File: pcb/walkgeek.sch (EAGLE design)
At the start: 124 parts, among them M1 NOKIA1100_VIBRATOR, X1 NOKIA1100_EXT_CONN, X2 MICROSD_CONN

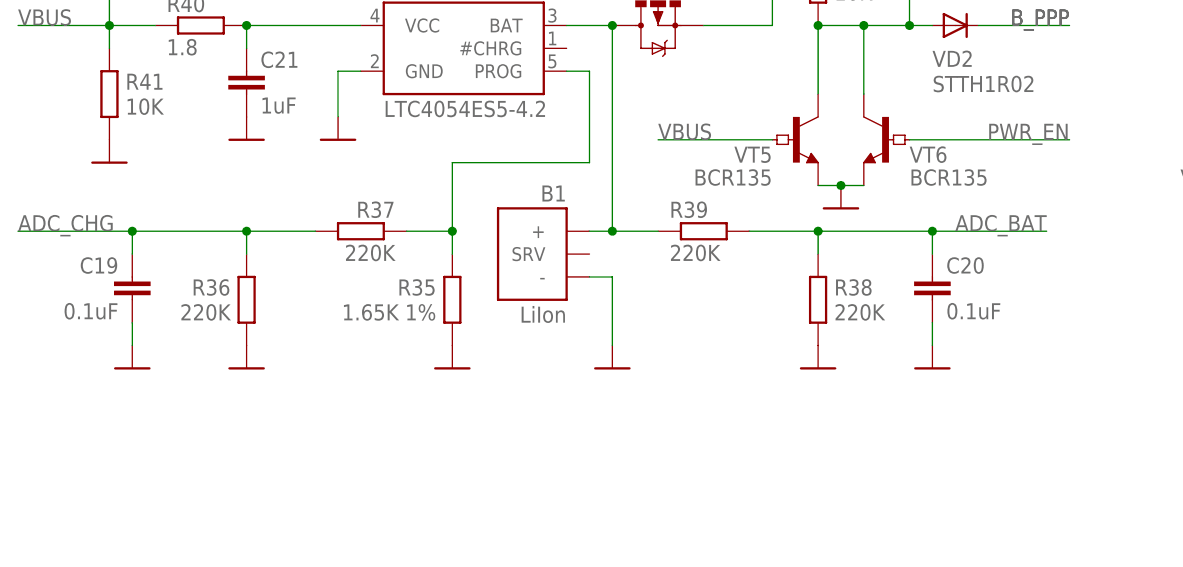
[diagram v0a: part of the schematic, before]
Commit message: Ported OPUS
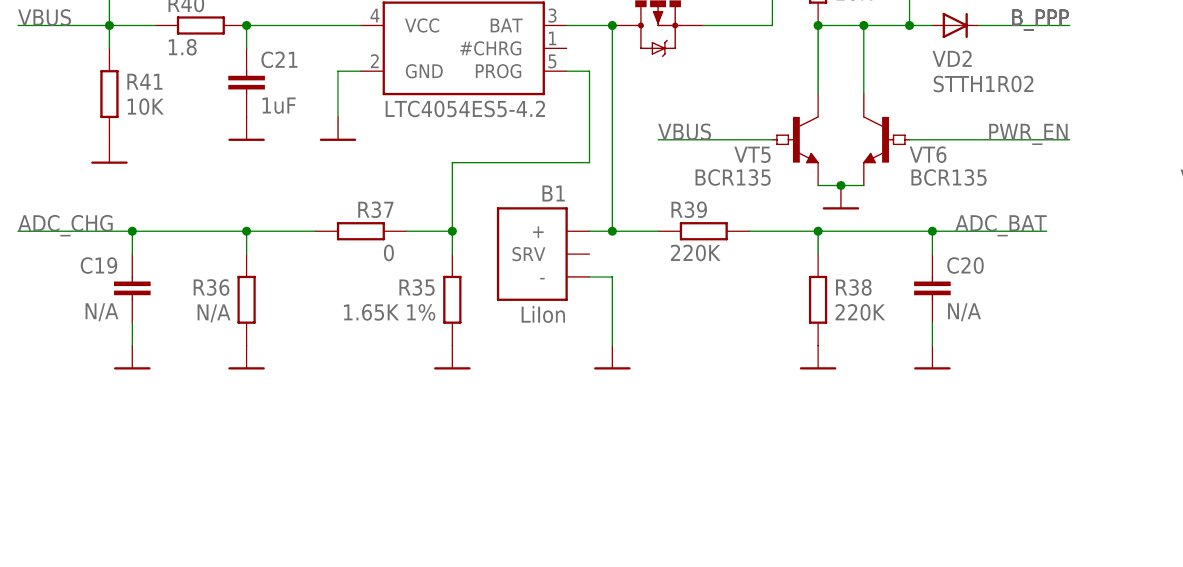
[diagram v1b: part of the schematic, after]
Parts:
- C19, C20: value 0.1uF -> N/A
- R36: value 220K -> N/A
- R37: value 220K -> 0
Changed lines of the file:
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@@
 <setting verticaltext="up"/>
 </settings>
-<grid distance="0.05" unitdist="inch" unit="inch" style="lines" multiple="1" display="no" altdistance="0.01" altunitdist="inch" altunit="inch"/>
+<grid distance="0.1" unitdist="inch" unit="inch" style="lines" multiple="1" display="no" altdistance="0.01" altunitdist="inch" altunit="inch"/>
 <layers>
 <layer number="1" name="Top" color="4" fill="1" visible="no" active="no"/>
@@
 <part name="DD3" library="walkgeek-eagle" deviceset="LTC4054ES5-4.2" device=""/>
 <part name="R35" library="walkgeek-eagle" deviceset="R-EU_" device="R0805" value="1.65K 1%"/>
-<part name="R36" library="walkgeek-eagle" deviceset="R-EU_" device="R0805" value="220K"/>
-<part name="R37" library="walkgeek-eagle" deviceset="R-EU_" device="R0805" value="220K"/>
+<part name="R36" library="walkgeek-eagle" deviceset="R-EU_" device="R0805" value="N/A"/>
+<part name="R37" library="walkgeek-eagle" deviceset="R-EU_" device="R0805" value="0"/>
 <part name="GND17" library="supply1" deviceset="GND" device=""/>
 <part name="GND19" library="supply1" deviceset="GND" device=""/>
 <part name="GND20" library="supply1" deviceset="GND" device=""/>
-<part name="C19" library="walkgeek-eagle" deviceset="C-EU" device="C0805" value="0.1uF"/>
+<part name="C19" library="walkgeek-eagle" deviceset="C-EU" device="C0805" value="N/A"/>
 <part name="GND21" library="supply1" deviceset="GND" device=""/>
 <part name="GND22" library="supply1" deviceset="GND" device=""/>
@@
 <part name="R39" library="walkgeek-eagle" deviceset="R-EU_" device="R0805" value="220K"/>
 <part name="GND23" library="supply1" deviceset="GND" device=""/>
-<part name="C20" library="walkgeek-eagle" deviceset="C-EU" device="C0805" value="0.1uF"/>
+<part name="C20" library="walkgeek-eagle" deviceset="C-EU" device="C0805" value="N/A"/>
 <part name="GND24" library="supply1" deviceset="GND" device=""/>
 <part name="C21" library="walkgeek-eagle" deviceset="C-EU" device="C0805" value="1uF"/>

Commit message: PowerManager fixes
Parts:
- removed C19, C20: N/A, walkgeek-eagle:C-EUC0805
- removed R36: N/A, walkgeek-eagle:R-EU_R0805
- removed R37: 0, walkgeek-eagle:R-EU_R0805
- R35: value 1.65K 1% -> 2K 1%
- R38, R39: value 220K -> 10K 1%
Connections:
- removed net N$15: DD3.PROG, R35.2, R37.1
- net ADC_BAT: no longer C20.1
- net ADC_CHG: now also DD3.PROG, R35.2; no longer C19.1, R36.2, R37.2
- net GND: no longer C19.2, C20.2, R36.1
- net N$17: now also R39.1
- net VBAT0: no longer R39.1
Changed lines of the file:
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@@
 <part name="R34" library="walkgeek-eagle" deviceset="R-EU_" device="R0805" value="47K"/>
 <part name="DD3" library="walkgeek-eagle" deviceset="LTC4054ES5-4.2" device=""/>
-<part name="R35" library="walkgeek-eagle" deviceset="R-EU_" device="R0805" value="1.65K 1%"/>
-<part name="R36" library="walkgeek-eagle" deviceset="R-EU_" device="R0805" value="N/A"/>
-<part name="R37" library="walkgeek-eagle" deviceset="R-EU_" device="R0805" value="0"/>
+<part name="R35" library="walkgeek-eagle" deviceset="R-EU_" device="R0805" value="2K 1%"/>
 <part name="GND17" library="supply1" deviceset="GND" device=""/>
-<part name="GND19" library="supply1" deviceset="GND" device=""/>
 <part name="GND20" library="supply1" deviceset="GND" device=""/>
-<part name="C19" library="walkgeek-eagle" deviceset="C-EU" device="C0805" value="N/A"/>
-<part name="GND21" library="supply1" deviceset="GND" device=""/>
 <part name="GND22" library="supply1" deviceset="GND" device=""/>
-<part name="R38" library="walkgeek-eagle" deviceset="R-EU_" device="R0805" value="220K"/>
-<part name="R39" library="walkgeek-eagle" deviceset="R-EU_" device="R0805" value="220K"/>
+<part name="R38" library="walkgeek-eagle" deviceset="R-EU_" device="R0805" value="10K 1%"/>
+<part name="R39" library="walkgeek-eagle" deviceset="R-EU_" device="R0805" value="10K 1%"/>
 <part name="GND23" library="supply1" deviceset="GND" device=""/>
-<part name="C20" library="walkgeek-eagle" deviceset="C-EU" device="C0805" value="N/A"/>
-<part name="GND24" library="supply1" deviceset="GND" device=""/>
 <part name="C21" library="walkgeek-eagle" deviceset="C-EU" device="C0805" value="1uF"/>
 <part name="GND25" library="supply1" deviceset="GND" device=""/>
@@
 <attribute name="VALUE" x="488.442" y="207.772" size="1.778" layer="96" rot="R180"/>
 </instance>
-<instance part="R36" gate="G$1" x="467.36" y="208.28" smashed="yes" rot="MR90">
-<attribute name="NAME" x="465.582" y="208.7626" size="1.778" layer="95" rot="MR0"/>
-<attribute name="VALUE" x="465.582" y="207.772" size="1.778" layer="96" rot="R180"/>
-</instance>
-<instance part="R37" gate="G$1" x="480.06" y="215.9" rot="MR0"/>
 <instance part="GND17" gate="1" x="490.22" y="200.66" smashed="yes" rot="MR0"/>
-<instance part="GND19" gate="1" x="467.36" y="200.66" smashed="yes" rot="MR0"/>
 <instance part="GND20" gate="1" x="477.52" y="226.06" smashed="yes"/>
-<instance part="C19" gate="G$1" x="454.66" y="210.82" rot="MR0"/>
-<instance part="GND21" gate="1" x="454.66" y="200.66" smashed="yes" rot="MR0"/>
 <instance part="GND22" gate="1" x="508" y="200.66" smashed="yes"/>
 <instance part="R38" gate="G$1" x="530.86" y="208.28" smashed="yes" rot="R90">
@@
 <instance part="R39" gate="G$1" x="518.16" y="215.9"/>
 <instance part="GND23" gate="1" x="530.86" y="200.66" smashed="yes"/>
-<instance part="C20" gate="G$1" x="543.56" y="210.82"/>
-<instance part="GND24" gate="1" x="543.56" y="200.66" smashed="yes"/>
 <instance part="C21" gate="G$1" x="467.36" y="233.68"/>
 <instance part="GND25" gate="1" x="467.36" y="226.06" smashed="yes"/>
@@
 </segment>
 <segment>
-<pinref part="R36" gate="G$1" pin="1"/>
-<pinref part="GND19" gate="1" pin="GND"/>
-</segment>
-<segment>
 <pinref part="DD3" gate="G$1" pin="GND"/>
 <wire x1="480.06" y1="233.68" x2="477.52" y2="233.68" width="0.1524" layer="91"/>
@@
 </segment>
 <segment>
-<pinref part="C19" gate="G$1" pin="2"/>
-<pinref part="GND21" gate="1" pin="GND"/>
-<wire x1="454.66" y1="203.2" x2="454.66" y2="205.74" width="0.1524" layer="91"/>
-</segment>
-<segment>
 <pinref part="B1" gate="B$1" pin="-"/>
 <wire x1="505.46" y1="210.82" x2="508" y2="210.82" width="0.1524" layer="91"/>
@@
 <pinref part="R38" gate="G$1" pin="1"/>
 <pinref part="GND23" gate="1" pin="GND"/>
-</segment>
-<segment>
-<pinref part="C20" gate="G$1" pin="2"/>
-<pinref part="GND24" gate="1" pin="GND"/>
-<wire x1="543.56" y1="203.2" x2="543.56" y2="205.74" width="0.1524" layer="91"/>
 </segment>
 <segment>
@@
 </segment>
 </net>
-<net name="N$15" class="0">
-<segment>
-<pinref part="R37" gate="G$1" pin="1"/>
+<net name="ADC_CHG" class="0">
+<segment>
+<wire x1="441.96" y1="215.9" x2="490.22" y2="215.9" width="0.1524" layer="91"/>
+<label x="441.96" y="215.9" size="1.778" layer="95"/>
 <pinref part="R35" gate="G$1" pin="2"/>
-<wire x1="490.22" y1="215.9" x2="485.14" y2="215.9" width="0.1524" layer="91"/>
 <wire x1="490.22" y1="213.36" x2="490.22" y2="215.9" width="0.1524" layer="91"/>
 <pinref part="DD3" gate="G$1" pin="PROG"/>
@@
 <junction x="490.22" y="215.9"/>
 </segment>
-</net>
-<net name="ADC_CHG" class="0">
-<segment>
-<pinref part="R37" gate="G$1" pin="2"/>
-<wire x1="474.98" y1="215.9" x2="467.36" y2="215.9" width="0.1524" layer="91"/>
-<pinref part="R36" gate="G$1" pin="2"/>
-<wire x1="467.36" y1="215.9" x2="467.36" y2="213.36" width="0.1524" layer="91"/>
-<pinref part="C19" gate="G$1" pin="1"/>
-<wire x1="454.66" y1="213.36" x2="454.66" y2="215.9" width="0.1524" layer="91"/>
-<wire x1="454.66" y1="215.9" x2="467.36" y2="215.9" width="0.1524" layer="91"/>
-<junction x="467.36" y="215.9"/>
-<wire x1="454.66" y1="215.9" x2="441.96" y2="215.9" width="0.1524" layer="91"/>
-<junction x="454.66" y="215.9"/>
-<label x="441.96" y="215.9" size="1.778" layer="95"/>
-</segment>
 <segment>
 <pinref part="DD2" gate=".1" pin="PB1"/>
@@
 <pinref part="R38" gate="G$1" pin="2"/>
 <wire x1="530.86" y1="215.9" x2="530.86" y2="213.36" width="0.1524" layer="91"/>
-<pinref part="C20" gate="G$1" pin="1"/>
-<wire x1="543.56" y1="213.36" x2="543.56" y2="215.9" width="0.1524" layer="91"/>
-<wire x1="543.56" y1="215.9" x2="530.86" y2="215.9" width="0.1524" layer="91"/>
 <junction x="530.86" y="215.9"/>
-<wire x1="543.56" y1="215.9" x2="556.26" y2="215.9" width="0.1524" layer="91"/>
-<junction x="543.56" y="215.9"/>
+<wire x1="530.86" y1="215.9" x2="556.26" y2="215.9" width="0.1524" layer="91"/>
 <label x="556.26" y="215.9" size="1.778" layer="95" rot="MR0"/>
 </segment>
@@
 <segment>
 <pinref part="B1" gate="B$1" pin="+"/>
-<pinref part="R39" gate="G$1" pin="1"/>
-<wire x1="513.08" y1="215.9" x2="508" y2="215.9" width="0.1524" layer="91"/>
 <wire x1="508" y1="215.9" x2="505.46" y2="215.9" width="0.1524" layer="91"/>
-<junction x="508" y="215.9"/>
 <pinref part="VT3" gate="VT$1" pin="D"/>
 <pinref part="DD3" gate="G$1" pin="BAT"/>
@@
 <wire x1="523.24" y1="248.92" x2="525.78" y2="248.92" width="0.1524" layer="91"/>
 <junction x="525.78" y="248.92"/>
-</segment>
-</net>
+<wire x1="525.78" y1="238.76" x2="525.78" y2="231.14" width="0.1524" layer="91"/>
+<junction x="525.78" y="238.76"/>
+<wire x1="525.78" y1="231.14" x2="510.54" y2="231.14" width="0.1524" layer="91"/>
+<wire x1="510.54" y1="231.14" x2="510.54" y2="215.9" width="0.1524" layer="91"/>
+<pinref part="R39" gate="G$1" pin="1"/>
+<wire x1="510.54" y1="215.9" x2="513.08" y2="215.9" width="0.1524" layer="91"/>
+</segment>
+</net>

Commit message: Updated README
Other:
- note added: "SWD"
- note removed: "Adjust backlight current"
- note removed: "I2C Address = 0011100b"
- note removed: "I2C Address = 0x94"
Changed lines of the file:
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@@
 <sheet>
 <plain>
-<text x="683.26" y="274.32" size="1.778" layer="98">I2C Address = 0011100b</text>
-<text x="510.54" y="274.32" size="1.778" layer="98">I2C Address = 0x94</text>
-<text x="775.97" y="323.85" size="1.778" layer="98" align="bottom-center">Adjust backlight current</text>
+<text x="716.28" y="223.52" size="1.778" layer="91">SWD</text>
 </plain>
 <instances>

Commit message: Corrected pcb numbering and captions
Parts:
- removed C52, C53, C54, C55, C65, C66: 0.1uF, walkgeek-eagle:C-EUC0402
- removed C63: 1uF, walkgeek-eagle:CPOL-EUSMCA
- removed C68, C69: 20pF, walkgeek-eagle:C-EUC0603
- removed R35: 2K 1%, walkgeek-eagle:R-EU_R0805
- removed R38, R39: 10K 1%, walkgeek-eagle:R-EU_R0805
- removed R40: 1.8, walkgeek-eagle:R-EU_R1206
- removed R41: 10K, walkgeek-eagle:R-EU_R0603
- removed R42: 10K, walkgeek-eagle:R-EU_R0805
- removed R51, R52: 4.7K, walkgeek-eagle:R-EU_R0603
- added C19, C27, C28: 1uF, walkgeek-eagle:C-EUC0603
- added C20, C31, C32: 0.1uF, walkgeek-eagle:C-EUC0402
- added C23, C24: 0.01uF, walkgeek-eagle:C-EUC0603
- added C29: 2.2uF, walkgeek-eagle:CPOL-EUSMCA
- added R10, R11: 51, walkgeek-eagle:R-EU_R0603
- added R13: 10K, walkgeek-eagle:R-EU_R0805
- added R14: 0, walkgeek-eagle:R-EU_R0603
- added R15: 1K, walkgeek-eagle:R-EU_R0805
- added R24, R26: 10K, walkgeek-eagle:R-EU_R0603
- added R25: 33(*), walkgeek-eagle:R-EU_R1206
- C10: value 150pF -> 1uF
- C11: value 150pF -> 0.022uF
- C12, C39, C42, C44, C7, C9: value 1uF -> 0.1uF; device walkgeek-eagle:C-EUC0603 -> walkgeek-eagle:C-EUC0402
- C13: value 0.022uF -> 150pF
- C15: value 1uF -> 150pF; device walkgeek-eagle:CPOL-EUSMCA -> walkgeek-eagle:C-EUC0603
- C16: device walkgeek-eagle:C-EUC0805 -> walkgeek-eagle:C-EUC0402
- C17, C18, C5: value 0.1uF -> 1uF; device walkgeek-eagle:C-EUC0402 -> walkgeek-eagle:C-EUC0603
- C21: value 1uF -> 0.1uF; device walkgeek-eagle:C-EUC0805 -> walkgeek-eagle:C-EUC0402
- C22: value 0.1uF -> 0.01uF; device walkgeek-eagle:C-EUC0402 -> walkgeek-eagle:C-EUC0805
- C25: value 0.01uF -> 2.2uF; device walkgeek-eagle:C-EUC0603 -> walkgeek-eagle:CPOL-EUSMCA
- C3: value 0.1uF -> 1uF; device walkgeek-eagle:C-EUC0402 -> walkgeek-eagle:C-EUC0805
- C35: value 0.1uF -> 20pF; device walkgeek-eagle:C-EUC0402 -> walkgeek-eagle:C-EUC0603
- C36: value 100pF -> 20pF; device walkgeek-eagle:C-EUC0805 -> walkgeek-eagle:C-EUC0603
- C37: device walkgeek-eagle:C-EUC0603 -> walkgeek-eagle:CPOL-EUSMCA
- C38, C43: value 0.01uF -> 0.1uF; device walkgeek-eagle:C-EUC0603 -> walkgeek-eagle:C-EUC0402
- C46: value 0.1uF -> 100pF; device walkgeek-eagle:C-EUC0402 -> walkgeek-eagle:C-EUC0805
- C47: value 0.01uF -> 0.1uF; device walkgeek-eagle:C-EUC0805 -> walkgeek-eagle:C-EUC0402
- C48: value 0.1uF -> 0.01uF; device walkgeek-eagle:C-EUC0402 -> walkgeek-eagle:C-EUC0603
- C49: value 2.2uF -> 0.1uF; device walkgeek-eagle:CPOL-EUSMCA -> walkgeek-eagle:C-EUC0402
- C50: value 2.2uF -> 0.1uF; device walkgeek-eagle:CPOL-EUSMCA -> walkgeek-eagle:C-EUC0805
- C6: value 0.1uF -> 1uF; device walkgeek-eagle:C-EUC0402 -> walkgeek-eagle:CPOL-EUSMCA
- DD1: value CS43L22 -> LTC4054ES5-4.2; device walkgeek-eagle:CS43L22 -> walkgeek-eagle:LTC4054ES5-4.2
- DD3: value LTC4054ES5-4.2 -> CS43L22; device walkgeek-eagle:LTC4054ES5-4.2 -> walkgeek-eagle:CS43L22
- DD4: value USBLC6-2SC6 -> LIS302DL; device walkgeek-eagle:USBLC6-2SC6 -> walkgeek-eagle:LIS302DL
- DD5: value LIS302DL -> USBLC6-2SC6; device walkgeek-eagle:LIS302DL -> walkgeek-eagle:USBLC6-2SC6
- R1: device walkgeek-eagle:R-EU_R0402 -> walkgeek-eagle:R-EU_R0603
- R2: value 51 -> 1.8; device walkgeek-eagle:R-EU_R0603 -> walkgeek-eagle:R-EU_R1206
- R3: value 51 -> 10K; device walkgeek-eagle:R-EU_R0603 -> walkgeek-eagle:R-EU_R0402
- R4: value 10K -> 4.7K; device walkgeek-eagle:R-EU_R0805 -> walkgeek-eagle:R-EU_R0603
- R5: value 0 -> 2K 1%; device walkgeek-eagle:R-EU_R0603 -> walkgeek-eagle:R-EU_R0805
- R6: value 1K -> 4.7K; device walkgeek-eagle:R-EU_R0805 -> walkgeek-eagle:R-EU_R0603
- R7: value 33(*) -> 10K 1%; device walkgeek-eagle:R-EU_R1206 -> walkgeek-eagle:R-EU_R0805
- R8: device walkgeek-eagle:R-EU_R0603 -> walkgeek-eagle:R-EU_R0805
- R9: value 10K -> 10K 1%; device walkgeek-eagle:R-EU_R0603 -> walkgeek-eagle:R-EU_R0805
- VT2, VT3: value IRLML6402 -> BCR135; device walkgeek-eagle:IRLML6402 -> walkgeek-eagle:VT_NPN_DIGITAL
- VT5, VT6: value BCR135 -> IRLML6402; device walkgeek-eagle:VT_NPN_DIGITAL -> walkgeek-eagle:IRLML6402
- renumbered C51 to C30, C62 to C26, C64 to C34, R29 to R18, R30 to R20, R31 to R21, R32 to R22, R33 to R23, R34 to R19, R55 to R12, R57 to R17, R59 to R16, ZQ2 to ZQ1
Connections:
- net #PRST: now also DD3.#RESET, R3.2; no longer DD1.#RESET, R1.2
- net +2V5: now also C27.1, C31.1, C4.1, C6.+, DD3.+VHP, DD3.VA, DD3.VD; no longer C15.+, C3.1, C39.1, C41.1, DD1.+VHP, DD1.VA, DD1.VD
- net +3V3: now also C12.1, C28.1, C32.1, C33.1, C38.1, C41.1, C42.1, C43.1, C45.1, C50.1, C7.1, C9.1, DD3.VL, DD3.VP, DD3.VP@1, DD4.CS.I2C_SPI, DD4.RESERVED, DD4.VDD, DD4.VDD_IO, R13.1, R4.2, R6.2; no longer C16.1, C18.1, C22.1, C35.1, C4.1, C46.1, C5.1, C52.1, C53.1, C54.1, C55.1, C6.1, DD1.VL, DD1.VP, DD1.VP@1, DD5.CS.I2C_SPI, DD5.RESERVED, DD5.VDD, DD5.VDD_IO, R4.1, R51.2, R52.2
- net ADC_BAT: now also R7.2, R9.2; no longer R38.2, R39.2
- net ADC_CHG: now also DD1.PROG, R5.2; no longer DD3.PROG, R35.2
- net BTN_ADC: now also C22.1, R13.2, R15.2; no longer C47.1, R4.2, R6.2
- net BTN_OUT: now also R15.1; no longer R6.1
- net B_0: now also SB11.INNER; no longer SB16.INNER
- net B_1: now also SB3.INNER; no longer SB6.INNER
- net B_2: now also SB8.INNER; no longer SB7.INNER
- net B_3: now also SB14.INNER; no longer SB8.INNER
- net B_4: now also SB4.INNER; no longer SB9.INNER
- net B_5: now also SB9.INNER; no longer SB10.INNER
- net B_6: now also SB15.INNER; no longer SB11.INNER
- net B_7: now also SB5.INNER; no longer SB12.INNER
- net B_8: now also SB10.INNER; no longer SB13.INNER
- net B_9: now also SB16.INNER; no longer SB14.INNER
- net B_AST: now also SB6.INNER; no longer SB15.INNER
- net B_DWN: now also SB13.INNER; no longer SB5.INNER
- net B_SEL: now also SB7.INNER; no longer SB4.INNER
- net B_UP: now also SB12.INNER; no longer SB3.INNER
- net D_NBKL: now also R26.2, VT6.G; no longer R9.2, VT1.G
- net GND: now also C13.2, C15.2, C19.2, C20.2, C23.2, C24.2, C25.-, C27.2, C28.2, C29.-, C31.2, C32.2, C36.2, C37.-, C46.1, C49.2, C50.2, C6.-, DD1.GND, DD3.AD0, DD3.AGND, DD3.DGND, DD3.GND/PAD, DD3.SPKR/HP, DD4.GND@1, DD4.GND@2, DD4.GND@3, DD4.RESERVED@1, DD4.SDO, R10.1, R11.1, R14.1, R9.1, VT2.E, VT3.E; no longer C11.2, C15.-, C25.2, C36.1, C37.2, C46.2, C49.-, C50.-, C52.2, C53.2, C54.2, C55.2, C6.2, C63.-, C65.2, C66.2, C68.2, C69.2, DD1.AD0, DD1.AGND, DD1.DGND, DD1.GND/PAD, DD1.SPKR/HP, DD3.GND, DD5.GND@1, DD5.GND@2, DD5.GND@3, DD5.RESERVED@1, DD5.SDO, R2.1, R35.1, R38.1, R41.1, VT5.E, VT6.E
- net I2S_MCK: now also DD3.MCLK; no longer DD1.MCLK
- net I2S_SCK: now also DD3.SCLK; no longer DD1.SCLK
- net I2S_SD: now also DD3.SDIN; no longer DD1.SDIN
- net I2S_WS: now also DD3.LRCK; no longer DD1.LRCK
- net MEMS_INT1: now also DD4.INT1; no longer DD5.INT1
- net MEMS_INT2: now also DD4.INT2; no longer DD5.INT2
- net MEMS_SCL: now also DD4.SCL_SPC; no longer DD5.SCL_SPC
- net MEMS_SDA: now also DD4.SDA_SDI_SDO; no longer DD5.SDA_SDI_SDO
- net N$1: now also R25.1; no longer R7.1
- net N$10: now also C5.1, DD3.-VHPFILT; no longer C7.1, DD1.-VHPFILT
- net N$11: now also R14.2; no longer R5.2
- net N$12: now also C11.2, R10.2; no longer C13.2, R2.2
- net N$13: now also R11.2; no longer R3.2
- net N$14: now also VT5.D; no longer VT2.D
- net N$16: now also C3.1, DD1.VCC, R2.2; no longer C21.1, DD3.VCC, R40.2
- net N$17: now also R7.1, R8.2, VT1.S; no longer R39.1, R42.2, VT3.S
- net N$19: now also R25.2, VT6.D; no longer R7.2, VT1.D
- net N$2: now also C10.1, DD3.FILT+; no longer C9.1, DD1.FILT+
- net N$21: now also R8.1, VT2.C, VT3.C; no longer R42.1, VT5.C, VT6.C
- net N$22: now also DD5.IO1.2; no longer DD4.IO1.2
- net N$29: now also DD5.IO2.2; no longer DD4.IO2.2
- net N$3: now also C13.1, DD3.AFILTA; no longer C10.1, DD1.AFILTA
- net N$31: now also C25.+; no longer C49.+
- net N$33: now also C35.1; no longer C69.1
- net N$34: now also C24.1; no longer C43.1
- net N$35: now also C23.1; no longer C38.1
- net N$38: now also C29.+; no longer C50.+
- net N$4: now also C15.1, DD3.AFILTB; no longer C11.1, DD1.AFILTB
- net N$40: now also C40.1; no longer C66.1
- net N$42: now also C37.+, C39.1; no longer C63.+, C65.1
- net N$44: now also C36.1; no longer C68.1
- net N$5: now also C19.1, DD3.VQ; no longer C12.1, DD1.VQ
- net N$6: now also C11.1, DD3.HP/LINE_OUTB; no longer C13.1, DD1.HP/LINE_OUTB
- net N$7: now also DD3.HP/LINE_OUTA; no longer DD1.HP/LINE_OUTA
- net N$8: now also DD3.FLYN; no longer DD1.FLYN
- net N$9: now also DD3.FLYP; no longer DD1.FLYP
- net NRST: now also C16.1; no longer C48.1
- net NVBTR: now also R24.2, VT5.G; no longer R8.2, VT2.G
- net PWR_EN: now also VT3.B; no longer VT6.B
- net SCL: now also DD3.SCL, R6.1; no longer DD1.SCL, R51.1
- net SDA: now also DD3.SDA, R4.1; no longer DD1.SDA, R52.1
- net SWCLK: now also C46.2; no longer C36.2
- net U_DM: now also DD5.IO2.1; no longer DD4.IO2.1
- net U_DP: now also DD5.IO1.1; no longer DD4.IO1.1
- net VBAT: now also C18.1, C20.1, C21.1, C47.1, R24.1, R26.1, VT5.S, VT6.S; no longer C37.1, C40.1, C42.1, C45.1, R8.1, R9.1, VT1.S, VT2.S
- net VBAT0: now also DD1.BAT, VT1.D; no longer DD3.BAT, VT3.D
- net VBUS: now also C48.1, C49.1, DD5.VBUS, R1.2, R2.1, VT1.G, VT2.B; no longer C25.1, C33.1, DD4.VBUS, R40.1, R41.2, VT3.G, VT5.B
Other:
- moved on the sheet: C10, C11, C12, C13, C16, C17, C18, C21, C22, C3, C33, C35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
